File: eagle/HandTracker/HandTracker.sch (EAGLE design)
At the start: 1 part

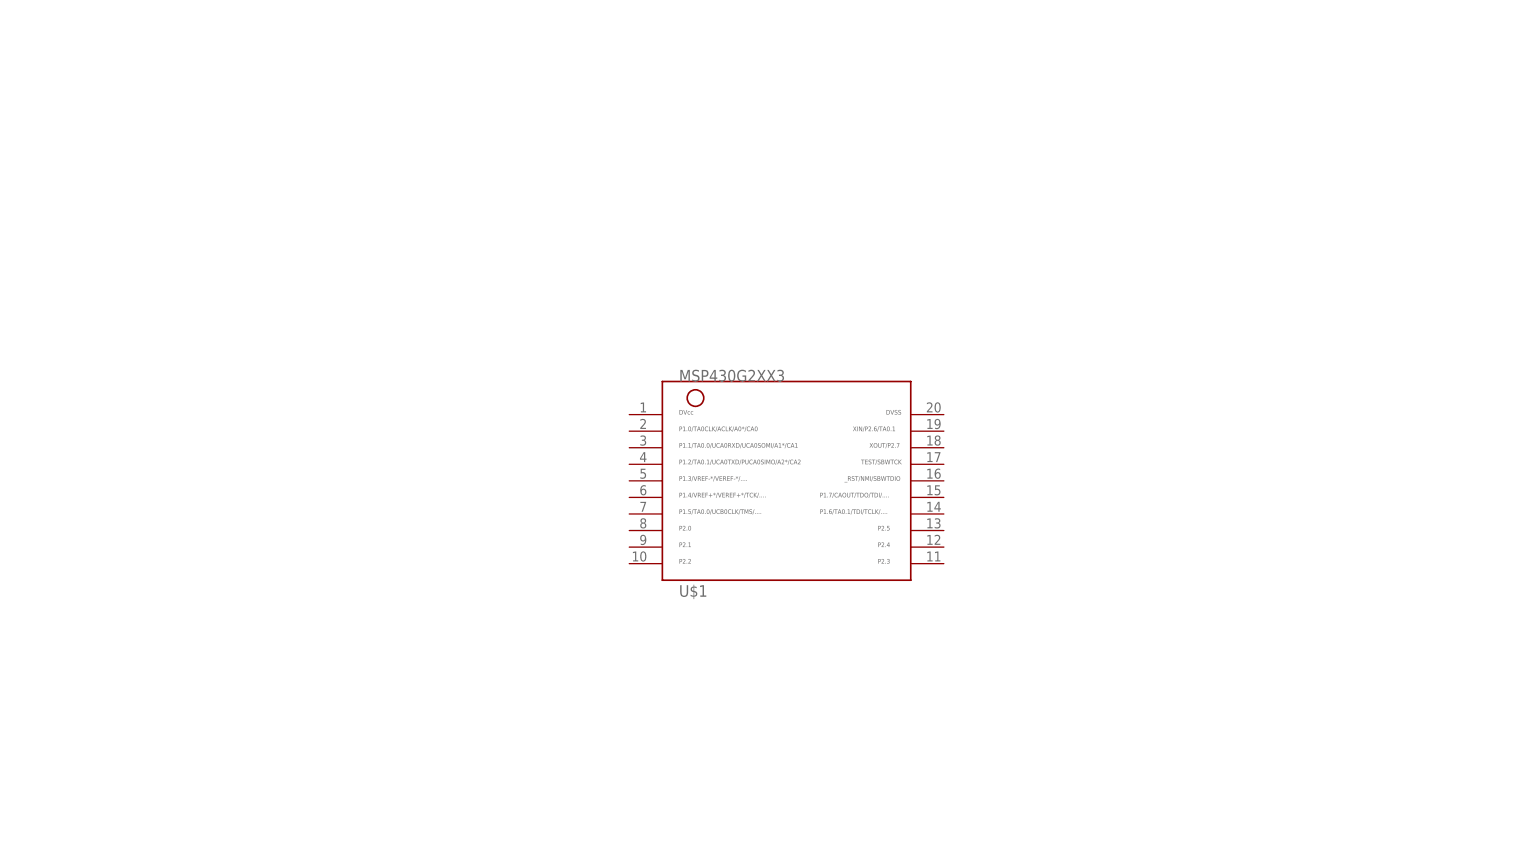
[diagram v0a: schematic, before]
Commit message: Started Populating Schematic with ICs
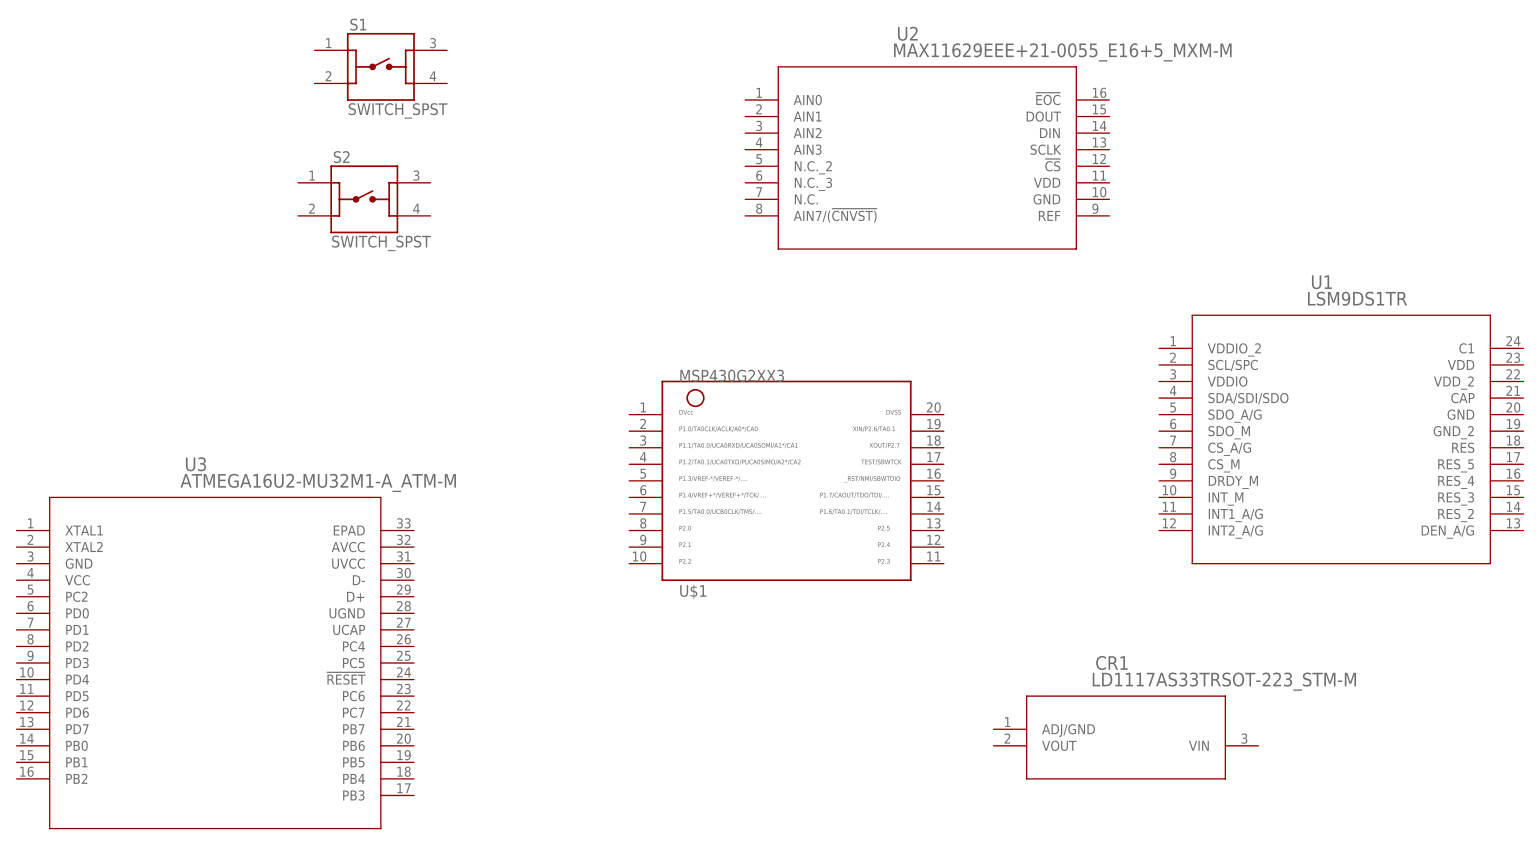
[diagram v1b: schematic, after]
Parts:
- added CR1: LD1117AS33TRSOT-223_STM-M, LD1117AS33TR:LD1117AS33TRSOT-223_STM-M
- added S1, S2: SWITCH_SPST, ELEC327:SWITCH_SPST
- added U1: LSM9DS1TR, LSM9DS1:LSM9DS1TR
- added U2: MAX11629EEE+21-0055_E16+5_MXM-M, MAX11629EEE+:MAX11629EEE+21-0055_E16+5_MXM-M
- added U3: ATMEGA16U2-MU32M1-A_ATM-M, AtMega16U2-MU:ATMEGA16U2-MU32M1-A_ATM-M
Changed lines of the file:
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@@
 <layer number="2" name="Route2" color="1" fill="3" visible="no" active="no"/>
 <layer number="3" name="Route3" color="4" fill="3" visible="no" active="no"/>
+<layer number="4" name="Route4" color="18" fill="1" visible="no" active="no"/>
+<layer number="5" name="Route5" color="19" fill="1" visible="no" active="no"/>
+<layer number="6" name="Route6" color="25" fill="1" visible="no" active="no"/>
+<layer number="7" name="Route7" color="26" fill="1" visible="no" active="no"/>
+<layer number="8" name="Route8" color="27" fill="1" visible="no" active="no"/>
+<layer number="9" name="Route9" color="28" fill="1" visible="no" active="no"/>
+<layer number="10" name="Route10" color="29" fill="1" visible="no" active="no"/>
+<layer number="11" name="Route11" color="30" fill="1" visible="no" active="no"/>
+<layer number="12" name="Route12" color="20" fill="1" visible="no" active="no"/>
+<layer number="13" name="Route13" color="21" fill="1" visible="no" active="no"/>
 <layer number="14" name="Route14" color="1" fill="6" visible="no" active="no"/>
 <layer number="15" name="Route15" color="4" fill="6" visible="no" active="no"/>
@@
 <parts>
 <part name="U$1" library="ELEC327" deviceset="MSP430G2XX3" device="TSSOP"/>
+<part name="CR1" library="LD1117AS33TR" deviceset="LD1117AS33TR" device="SOT-223_STM-M"/>
+<part name="U1" library="LSM9DS1" deviceset="LSM9DS1TR" device=""/>
+<part name="U2" library="MAX11629EEE+" deviceset="MAX11629EEE+" device="21-0055_E16+5_MXM-M"/>
+<part name="S1" library="ELEC327" deviceset="SWITCH_SPST" device=""/>
+<part name="S2" library="ELEC327" deviceset="SWITCH_SPST" device=""/>
+<part name="U3" library="AtMega16U2-MU" deviceset="ATMEGA16U2-MU" device="32M1-A_ATM-M"/>
 </parts>
 <sheets>
@@
 <attribute name="NAME" x="12.7" y="45.72" size="1.778" layer="95"/>
 </instance>
+<instance part="CR1" gate="A" x="58.42" y="25.4" smashed="yes">
+<attribute name="NAME" x="76.5556" y="34.5186" size="2.0828" layer="95" ratio="6" rot="SR0"/>
+<attribute name="VALUE" x="75.9206" y="31.9786" size="2.0828" layer="96" ratio="6" rot="SR0"/>
+</instance>
+<instance part="U1" gate="A" x="83.82" y="83.82" smashed="yes">
+<attribute name="NAME" x="109.5756" y="92.9386" size="2.0828" layer="95" ratio="6" rot="SR0"/>
+<attribute name="VALUE" x="108.9406" y="90.3986" size="2.0828" layer="96" ratio="6" rot="SR0"/>
+</instance>
+<instance part="U2" gate="A" x="20.32" y="121.92" smashed="yes">
+<attribute name="NAME" x="46.0756" y="131.0386" size="2.0828" layer="95" ratio="6" rot="SR0"/>
+<attribute name="VALUE" x="45.4406" y="128.4986" size="2.0828" layer="96" ratio="6" rot="SR0"/>
+</instance>
+<instance part="S1" gate="G$1" x="-33.02" y="127" smashed="yes">
+<attribute name="NAME" x="-37.8512" y="132.59401875" size="1.77991875" layer="95"/>
+<attribute name="VALUE" x="-38.104840625" y="119.626990625" size="1.779690625" layer="96"/>
+</instance>
+<instance part="S2" gate="G$1" x="-35.56" y="106.68" smashed="yes">
+<attribute name="NAME" x="-40.3912" y="112.27401875" size="1.77991875" layer="95"/>
+<attribute name="VALUE" x="-40.644840625" y="99.306990625" size="1.779690625" layer="96"/>
+</instance>
+<instance part="U3" gate="A" x="-91.44" y="55.88" smashed="yes">
+<attribute name="NAME" x="-63.1444" y="64.9986" size="2.0828" layer="95" ratio="6" rot="SR0"/>
+<attribute name="VALUE" x="-63.7794" y="62.4586" size="2.0828" layer="96" ratio="6" rot="SR0"/>
+</instance>
 </instances>

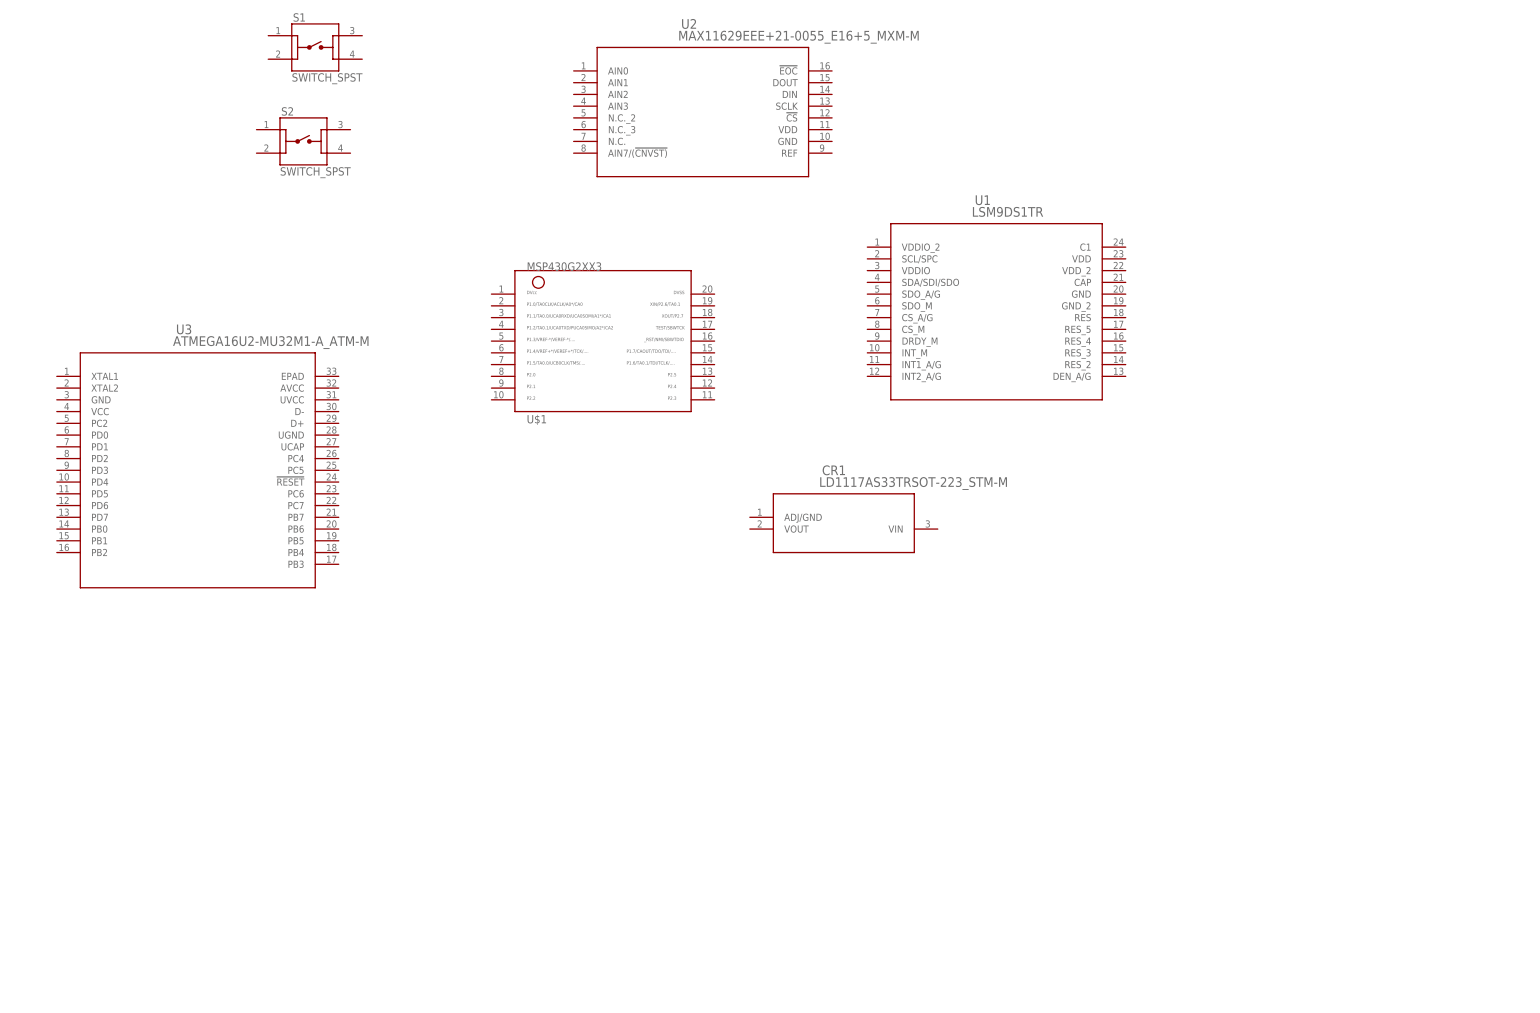
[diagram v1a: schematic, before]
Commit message: Continued Populating Schematic and began making connections
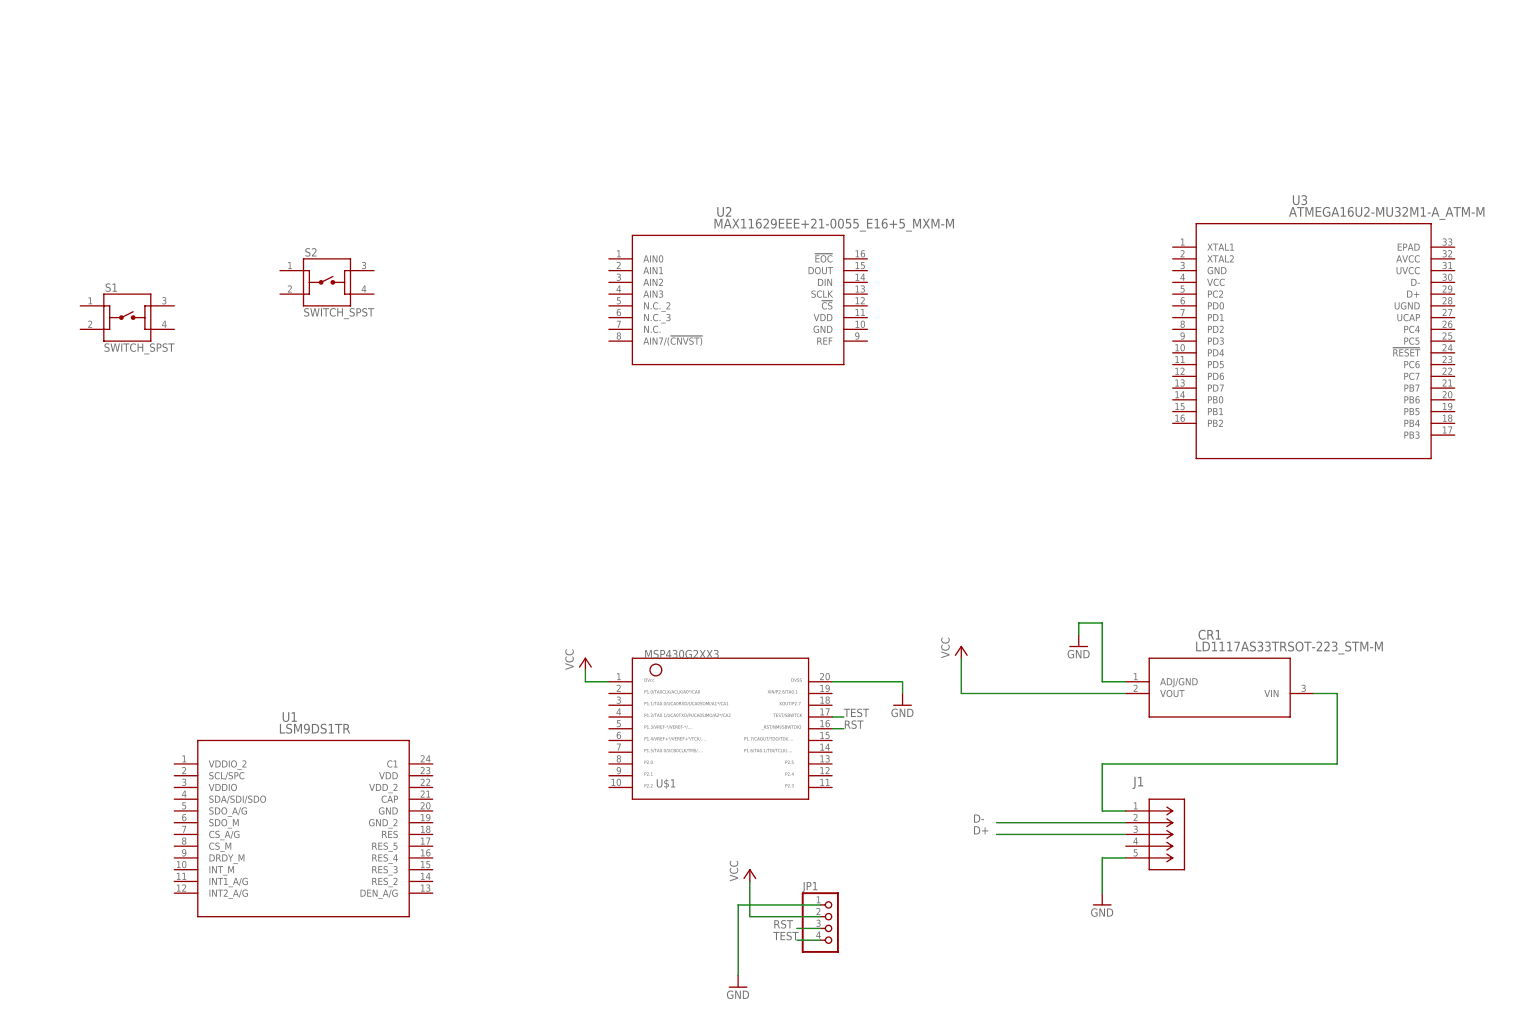
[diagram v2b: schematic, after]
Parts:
- added J1: ZX62-AB-5PA(31), USBHousing:ZX62-AB-5PA(31)
- added JP1: (no value), pinhead:PINHD-1X4/90
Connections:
- new net D+: J1.D+
- new net D-: J1.D-
- new net GND: CR1.ADJ/GND, J1.GND, JP1.1, U$1.20
- new net N$3: CR1.VIN, J1.VCC
- new net RST: JP1.3, U$1.16
- new net TEST: JP1.4, U$1.17
- new net VCC: CR1.VOUT, JP1.2, U$1.1
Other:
- moved on the sheet: CR1, S1, S2, U$1, U1, U2, U3
